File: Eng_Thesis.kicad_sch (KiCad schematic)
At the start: 0 parts

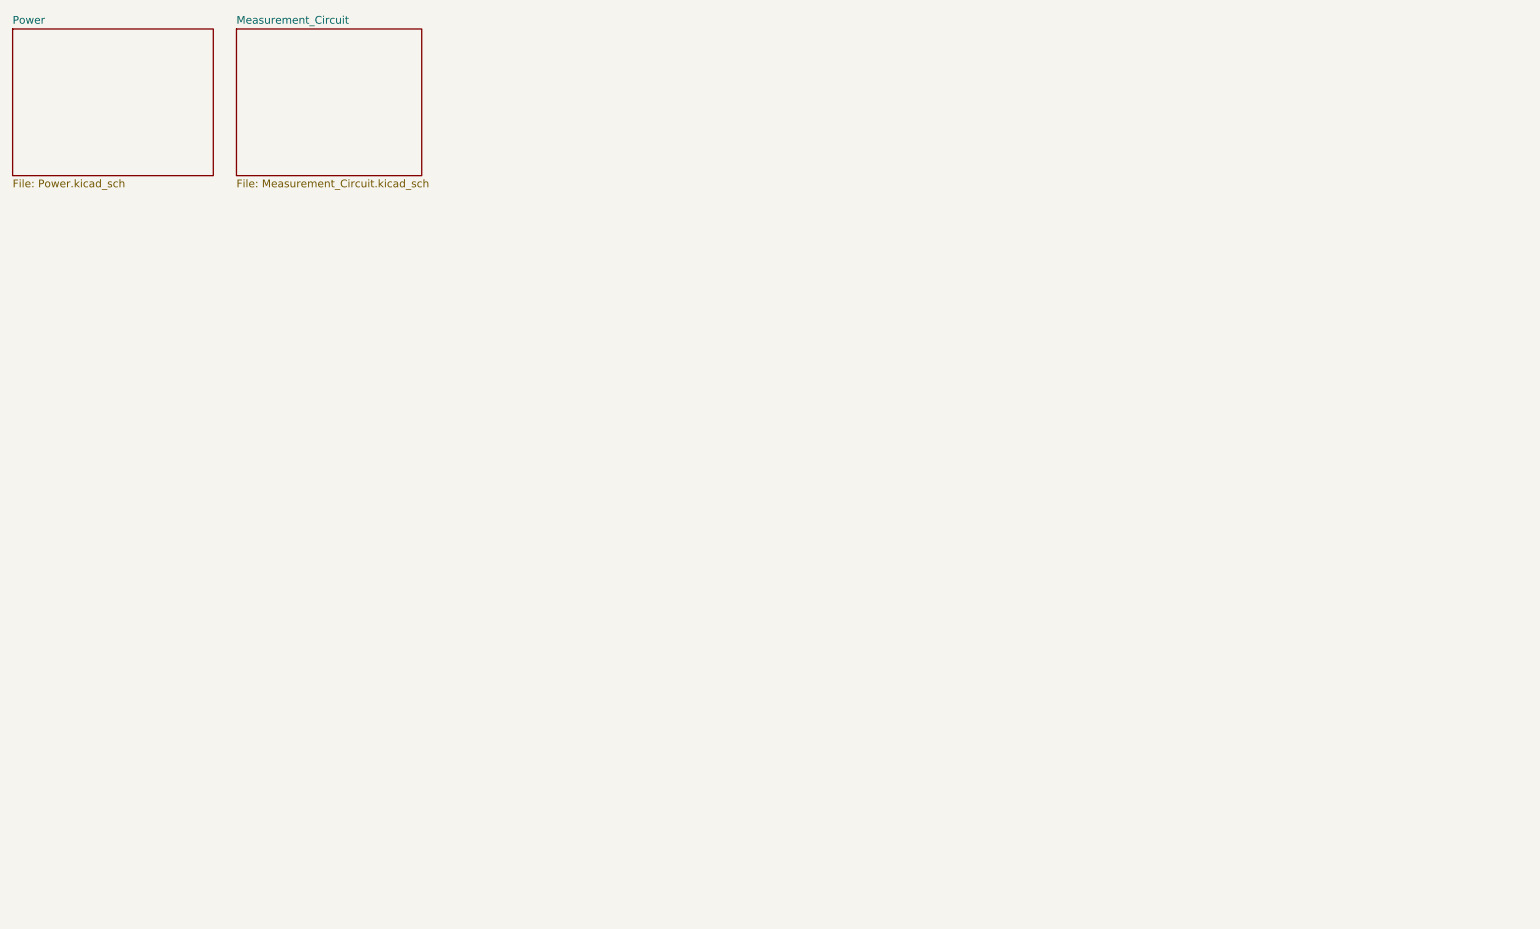
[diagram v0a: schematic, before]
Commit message: Microcontroller draft
Created a draft of the things connected to the microcontroller.
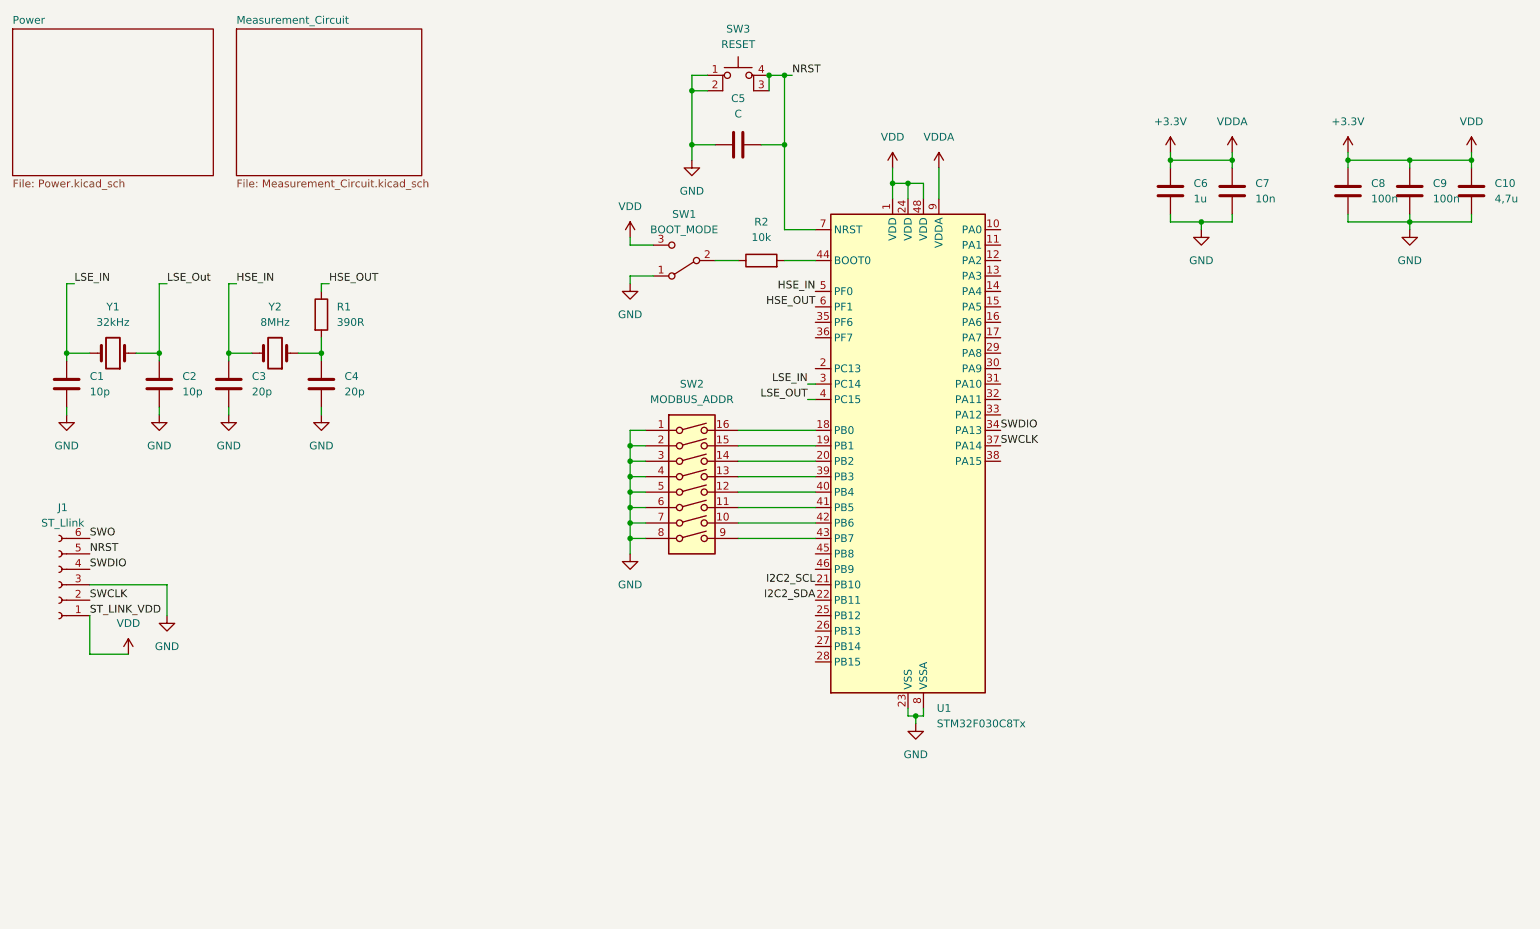
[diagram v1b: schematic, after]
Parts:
- added C1, C2: 10p, symbol Device:C
- added C10: 4,7u, symbol Device:C
- added C3, C4: 20p, symbol Device:C
- added C5: C, symbol Device:C
- added C6: 1u, symbol Device:C
- added C7: 10n, symbol Device:C
- added C8, C9: 100n, symbol Device:C
- added J1: ST_Llink, Connector_PinHeader_2.54mm:PinHeader_1x06_P2.54mm_Vertical, symbol Connector:Conn_01x06_Socket
- added R1: 390R, symbol Device:R
- added R2: 10k, symbol Device:R
- added SW1: BOOT_MODE, symbol Switch:SW_SPDT
- added SW2: MODBUS_ADDR, symbol Switch:SW_DIP_x08
- added SW3: RESET, symbol Switch:SW_MEC_5E
- added U1: STM32F030C8Tx, Package_QFP:LQFP-48_7x7mm_P0.5mm, symbol MCU_ST_STM32F0:STM32F030C8Tx
- added Y1: 32kHz, symbol Device:Crystal
- added Y2: 8MHz, symbol Device:Crystal
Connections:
- new net: C4.1, R1.2, Y2.1
- new net: SW2.16, U1.18 (PB0)
- new net: SW2.15, U1.19 (PB1)
- new net: SW2.14, U1.20 (PB2)
- new net: SW2.13, U1.39 (PB3)
- new net: SW2.12, U1.40 (PB4)
- new net: SW2.11, U1.41 (PB5)
- new net: SW2.10, U1.42 (PB6)
- new net: SW2.9, U1.43 (PB7)
- new net: R2.2, U1.44 (BOOT0)
- new net: R2.1, SW1.2 (B)
- new net +3.3V: C10.1, C6.1, C7.1, C8.1, C9.1, J1.1 (Pin_1), SW1.3 (C), U1.1 (VDD), U1.24 (VDD), U1.48 (VDD), U1.9 (VDDA)
- new net GND: C1.2, C10.2, C2.2, C3.2, C4.2, C5.1, C6.2, C7.2, C8.2, C9.2, J1.3 (Pin_3), SW1.1 (A), SW2.1, SW2.2, SW2.3, SW2.4, SW2.5, SW2.6, SW2.7, SW2.8, SW3.1, SW3.2, U1.23 (VSS), U1.47 (VSS), U1.8 (VSSA)
- new net HSE_IN: C3.1, U1.5 (PF0), Y2.2
- new net HSE_OUT: R1.1, U1.6 (PF1)
- new net I2C2_SCL: U1.21 (PB10)
- new net I2C2_SDA: U1.22 (PB11)
- new net LSE_IN: C1.1, U1.3 (PC14), Y1.2
- new net LSE_OUT: U1.4 (PC15)
- new net LSE_Out: C2.1, Y1.1
- new net NRST: C5.2, J1.5 (Pin_5), SW3.3 (K), SW3.4 (A), U1.7 (NRST)
- new net SWCLK: J1.2 (Pin_2), U1.37 (PA14)
- new net SWDIO: J1.4 (Pin_4), U1.34 (PA13)
- new net SWO: J1.6 (Pin_6)

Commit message: Partial measurement block
Added capacitor in Power, fixed the debug junction, added initial draft of measurement block
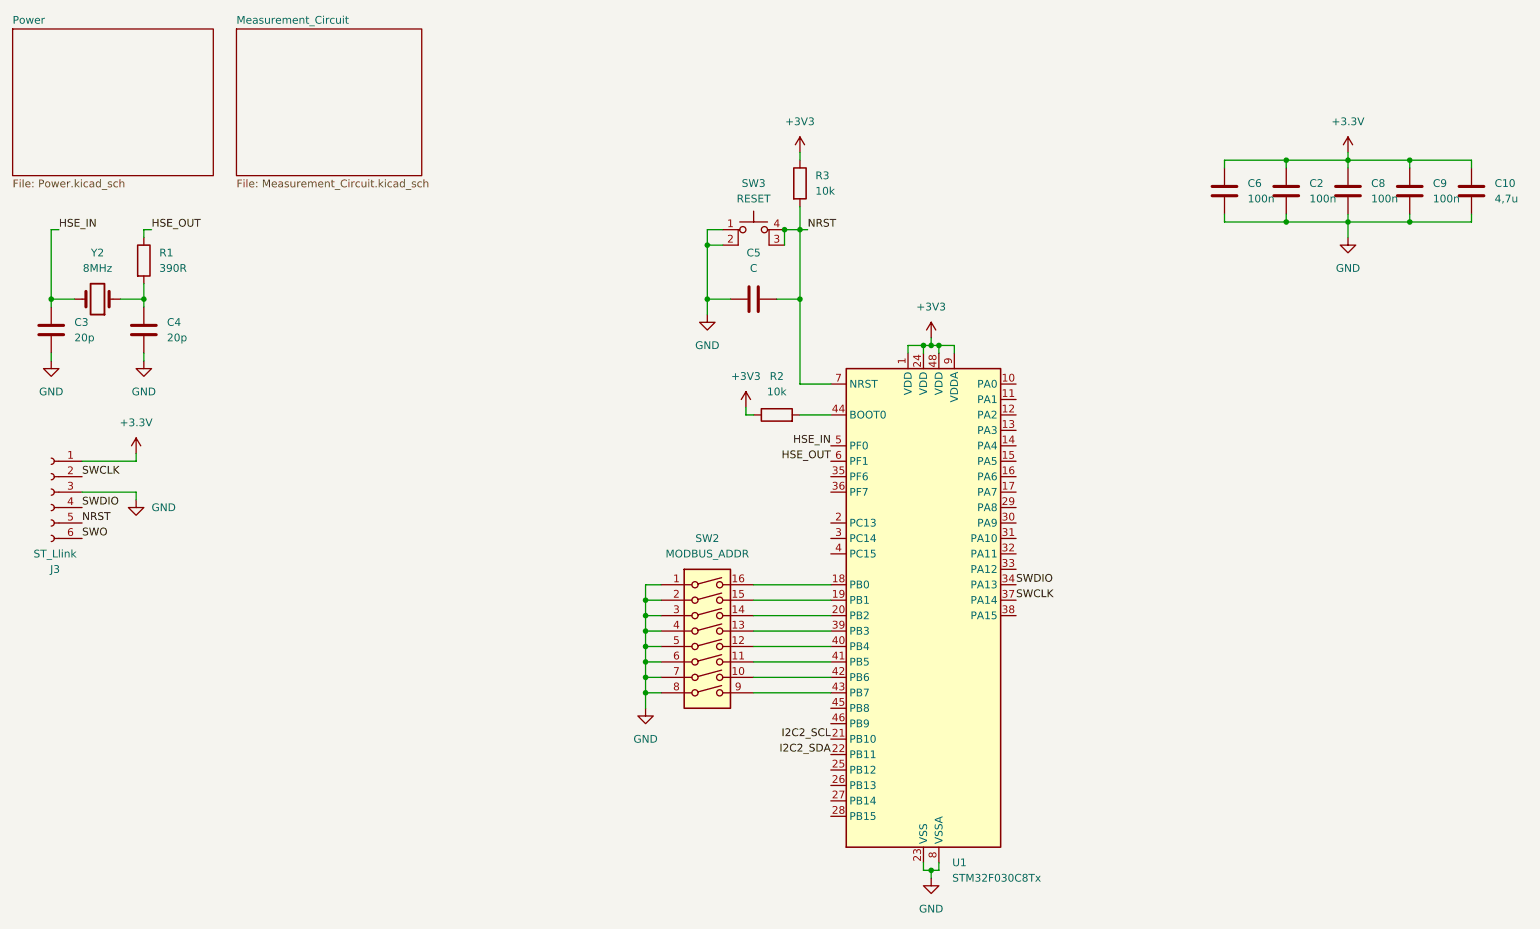
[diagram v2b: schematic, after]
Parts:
- removed C1: 10p, symbol Device:C
- removed C7: 10n, symbol Device:C
- removed J1: ST_Llink, Connector_PinHeader_2.54mm:PinHeader_1x06_P2.54mm_Vertical, symbol Connector:Conn_01x06_Socket
- removed SW1: BOOT_MODE, symbol Switch:SW_SPDT
- removed Y1: 32kHz, symbol Device:Crystal
- added J3: ST_Llink, Connector_PinHeader_2.54mm:PinHeader_1x06_P2.54mm_Vertical, symbol Connector:Conn_01x06_Socket
- added R3: 10k, symbol Device:R
- C2: value 10p -> 100n
- C6: value 1u -> 100n
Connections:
- net LSE_Out is gone; now on net +3.3V: C2.1
- net +3.3V: now also J3.1 (Pin_1); no longer U1.1 (VDD), U1.24 (VDD), U1.48 (VDD), U1.9 (VDDA)
- net GND: now also J3.3 (Pin_3)
- net NRST: now also J3.5 (Pin_5), R3.2
- net SWCLK: now also J3.2 (Pin_2)
- net SWDIO: now also J3.4 (Pin_4)
- net SWO: now also J3.6 (Pin_6)
- net +3V3: now reaches R2.1
- net +3V3: now also U1.1 (VDD), U1.24 (VDD), U1.48 (VDD), U1.9 (VDDA), R3.1
- net LSE_IN: no longer names the net of U1.3 (PC14)
- net LSE_OUT: no longer names the net of U1.4 (PC15)
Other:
- moved on the sheet: C3, C4, C5, R1, R2, SW2, SW3, U1, Y2
